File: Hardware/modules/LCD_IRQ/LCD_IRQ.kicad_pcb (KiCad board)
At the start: 4 copper layers, 83.3 x 68.2 mm, 23 parts, among them J1 Bus_PCI_6502, U1 74HC138, U2 W65C22SxP

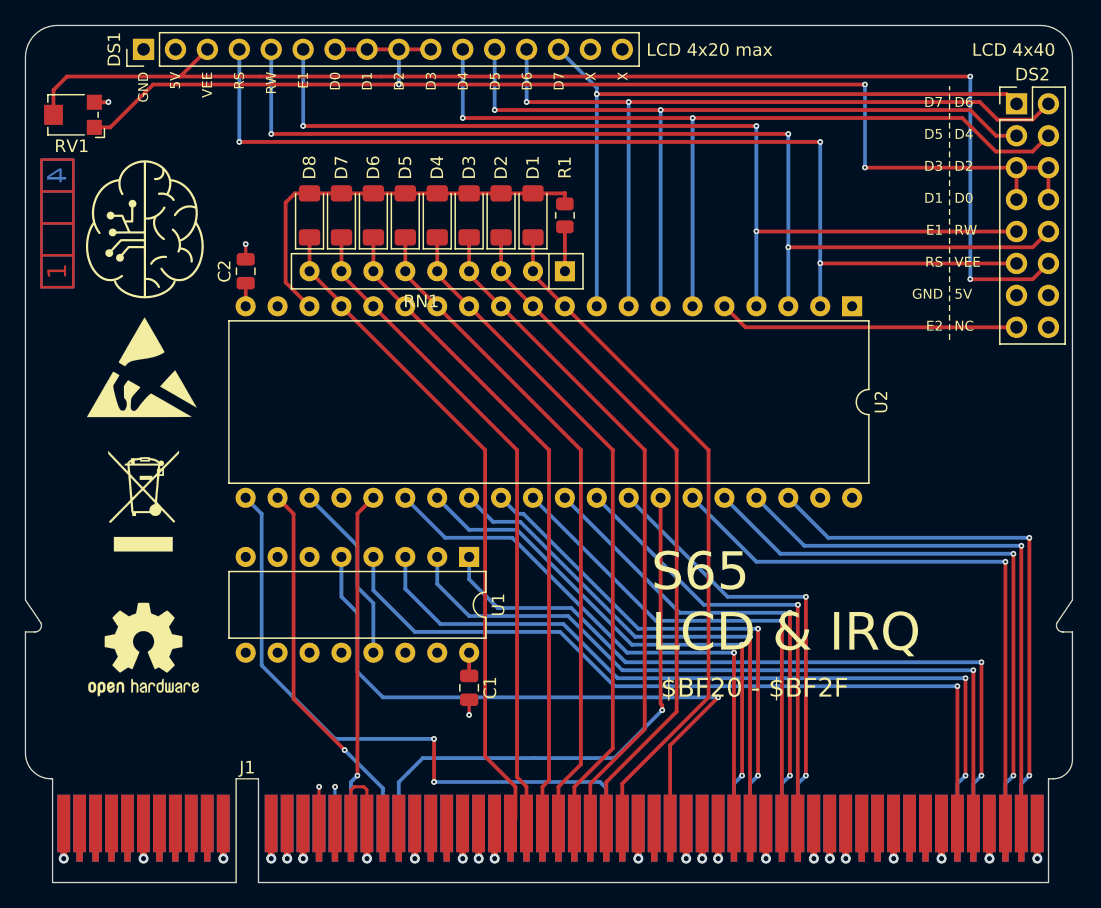
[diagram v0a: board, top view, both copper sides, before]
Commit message: Hardware Review Pt. 1 fix Address Decoding for Strobe Generators add bulk capacitance to every board fix wiring of Prototyping Board
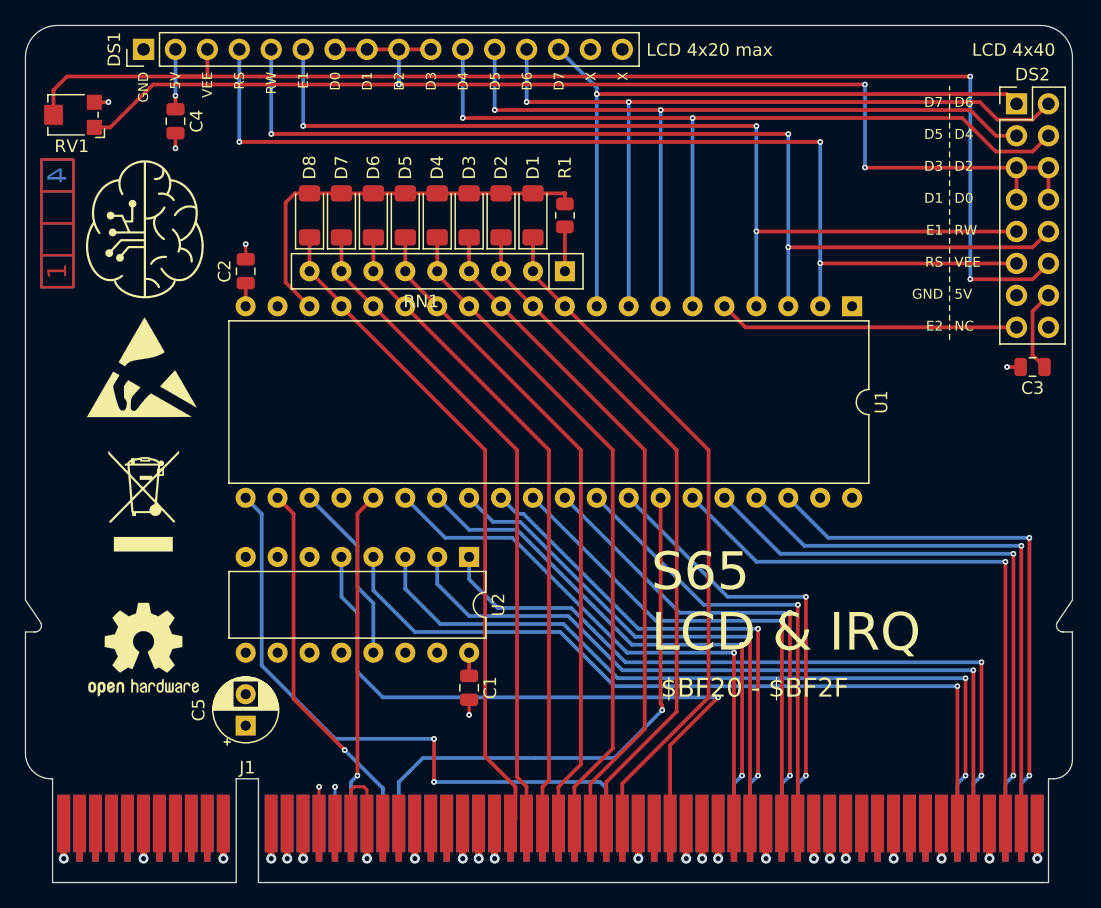
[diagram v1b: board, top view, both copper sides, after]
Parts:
- added C3: 4µ7, Capacitor_SMD:C_0805_2012Metric, F.Cu at (179.6, 86.0)
- added C4: 4µ7, Capacitor_SMD:C_0805_2012Metric, F.Cu at (111.4, 66.4)
- added C5: 10µ, Capacitor_THT:CP_Radial_D5.0mm_P2.50mm, F.Cu at (117.0, 114.5)
- renumbered U2 to U1, U1 to U2
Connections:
- J1 pad A11: /A13 -> unconnected-(J1-A13-PadA11)_0
- J1 pad A12: /A15 -> unconnected-(J1-A15-PadA12)_0
- J1 pad A25: /~{ROM} -> unconnected-(J1-~{ROM}-PadA25)_0
- J1 pad A38: /SYNC_VPA -> unconnected-(J1-Sync/VPA-PadA38)
- J1 pad A39: /Ø2/VDA -> unconnected-(J1-Ø2/VDA-PadA39)
- J1 pad A41: /~{RDY} -> unconnected-(J1-~{RDY}-PadA41)
- J1 pad A42: /~{BE} -> unconnected-(J1-~{BE}-PadA42)_0
- J1 pad A45: /E -> unconnected-(J1-E-PadA45)_0
- J1 pad A53: /RAM_0 -> unconnected-(J1-RAM0-PadA53)_0
- J1 pad A54: /RAM_1 -> unconnected-(J1-RAM1-PadA54)_0
- J1 pad A55: /RAM_2 -> unconnected-(J1-RAM2-PadA55)_0
- J1 pad A56: /RAM_3 -> unconnected-(J1-RAM3-PadA56)_0
- J1 pad A58: /RAM_4 -> unconnected-(J1-RAM4-PadA58)
- J1 pad A59: /RAM_5 -> unconnected-(J1-RAM5-PadA59)_0
- J1 pad A60: /RAM_6 -> unconnected-(J1-RAM6-PadA60)
- J1 pad A61: /RAM_7 -> unconnected-(J1-RAM7-PadA61)_0
- J1 pad A8: /A9 -> unconnected-(J1-A9-PadA8)_0
- J1 pad A9: /A11 -> unconnected-(J1-A11-PadA9)_0
- J1 pad B11: /A12 -> unconnected-(J1-A12-PadB11)_0
- J1 pad B12: /A14 -> unconnected-(J1-A14-PadB12)
- J1 pad B24: /~{L_RAM} -> unconnected-(J1-~{L_RAM}-PadB24)_0
- J1 pad B25: /~{H_RAM} -> unconnected-(J1-~{H_RAM}-PadB25)_0
- J1 pad B27: /~{IRQ} -> unconnected-(J1-~{IRQ}-PadB27)
- J1 pad B29: /~{IRQ_1} -> unconnected-(J1-~{IRQ_1}-PadB29)_0
- J1 pad B30: /~{IRQ_2} -> unconnected-(J1-~{IRQ_2}-PadB30)
- J1 pad B31: /~{IRQ_3} -> unconnected-(J1-~{IRQ_3}-PadB31)
- J1 pad B32: /~{IRQ_4} -> unconnected-(J1-~{IRQ_4}-PadB32)
- J1 pad B33: /~{NMI} -> unconnected-(J1-~{NMI}-PadB33)
- J1 pad B34: /PAGE -> unconnected-(J1-PAGE_ROM-PadB34)_0
- J1 pad B38: /~{VP} -> unconnected-(J1-~{VP}-PadB38)_0
- J1 pad B39: /~{ML} -> unconnected-(J1-~{ML}-PadB39)
- J1 pad B46: /M/X -> unconnected-(J1-M/~{X}-PadB46)
- J1 pad B53: /ROM_0 -> unconnected-(J1-ROM0-PadB53)
- J1 pad B54: /ROM_1 -> unconnected-(J1-ROM1-PadB54)_0
- J1 pad B55: /ROM_2 -> unconnected-(J1-ROM2-PadB55)
- J1 pad B56: /ROM_3 -> unconnected-(J1-ROM3-PadB56)
- J1 pad B58: /ROM_4 -> unconnected-(J1-ROM4-PadB58)_0
- J1 pad B59: /ROM_5 -> unconnected-(J1-ROM5-PadB59)_0
- J1 pad B60: /ROM_6 -> unconnected-(J1-ROM6-PadB60)_0
- J1 pad B61: /ROM_7 -> unconnected-(J1-ROM7-PadB61)
- J1 pad B8: /A8 -> unconnected-(J1-A8-PadB8)_0
- J1 pad B9: /A10 -> unconnected-(J1-A10-PadB9)
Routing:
- net +5V: track 7.22 -> 18.6 mm, vias 4 -> 5
- net GND: track 16.2 -> 18.5 mm, vias 23 -> 25
- net /VEE: track 101.3 -> 102.6 mm

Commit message: Big Review Update - Changed Copper Pours on all PCBs - Implemented errors found at review - fixed some additional errors
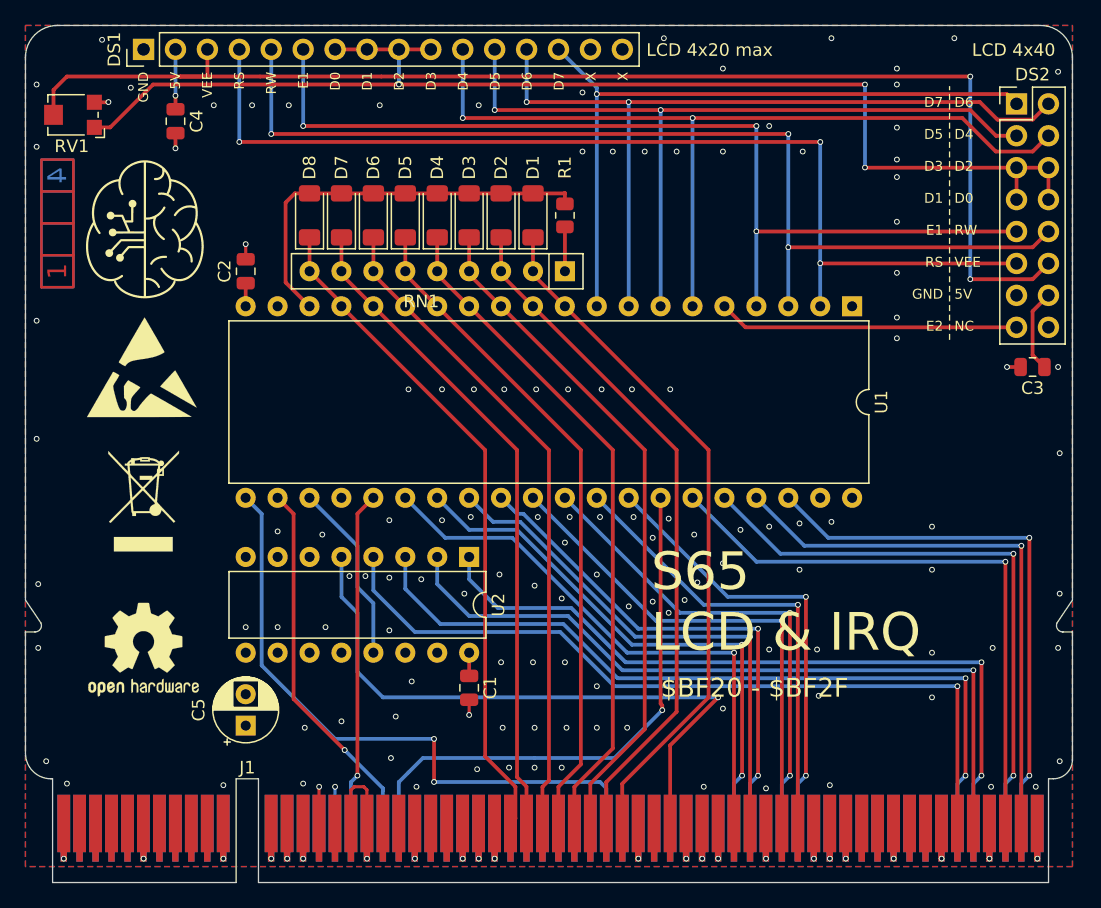
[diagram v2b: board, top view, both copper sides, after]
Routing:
- net +5V: vias 5 -> 128
- added copper zone on B.Cu, net +5V
- added copper zone on F.Cu, net +5V
- added copper zone on In1.Cu, net GND
- removed copper zone on In1.Cu, net +5V
